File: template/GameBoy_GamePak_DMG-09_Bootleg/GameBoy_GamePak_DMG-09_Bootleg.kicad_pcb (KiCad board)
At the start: 2 copper layers, 53 x 60.7 mm, 1 part, among them J1 GameBoy_GamePak_DMG-09

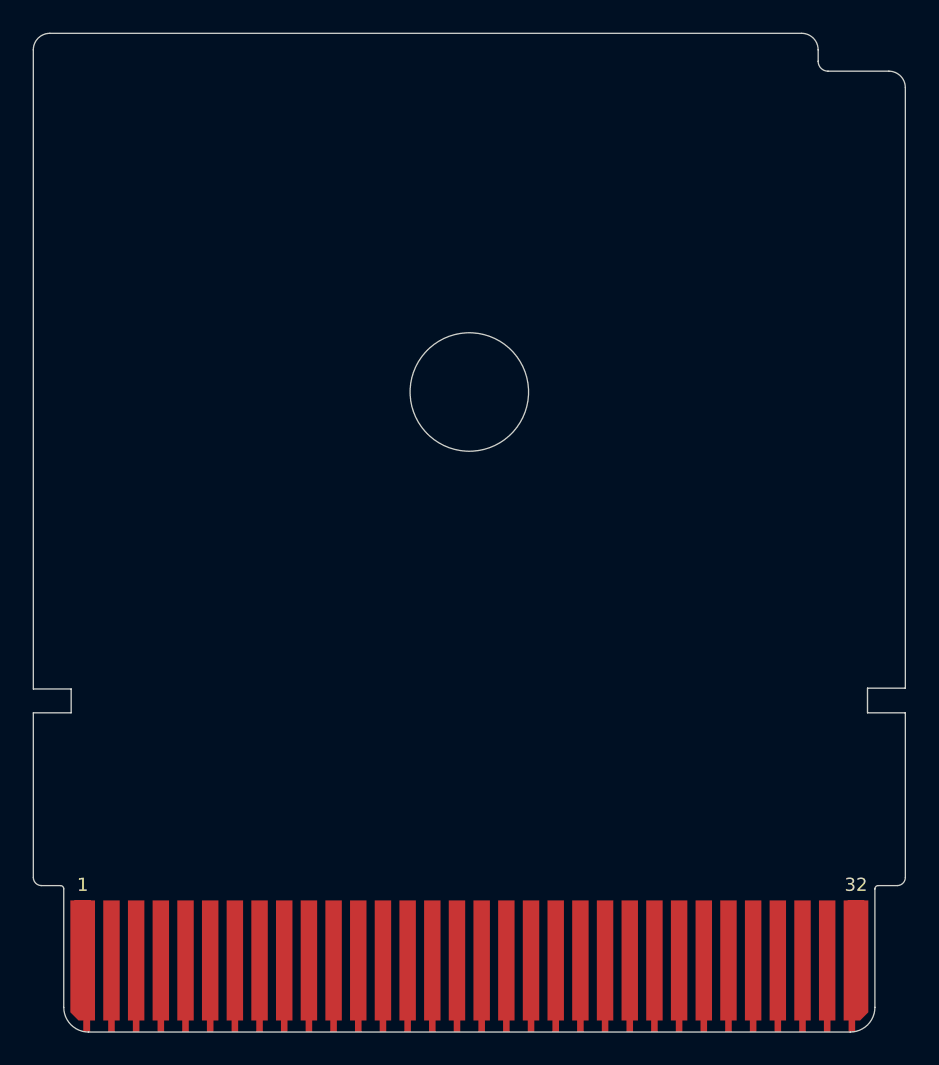
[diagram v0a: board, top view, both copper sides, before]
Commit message: Update all files to KiCAD 6.x format
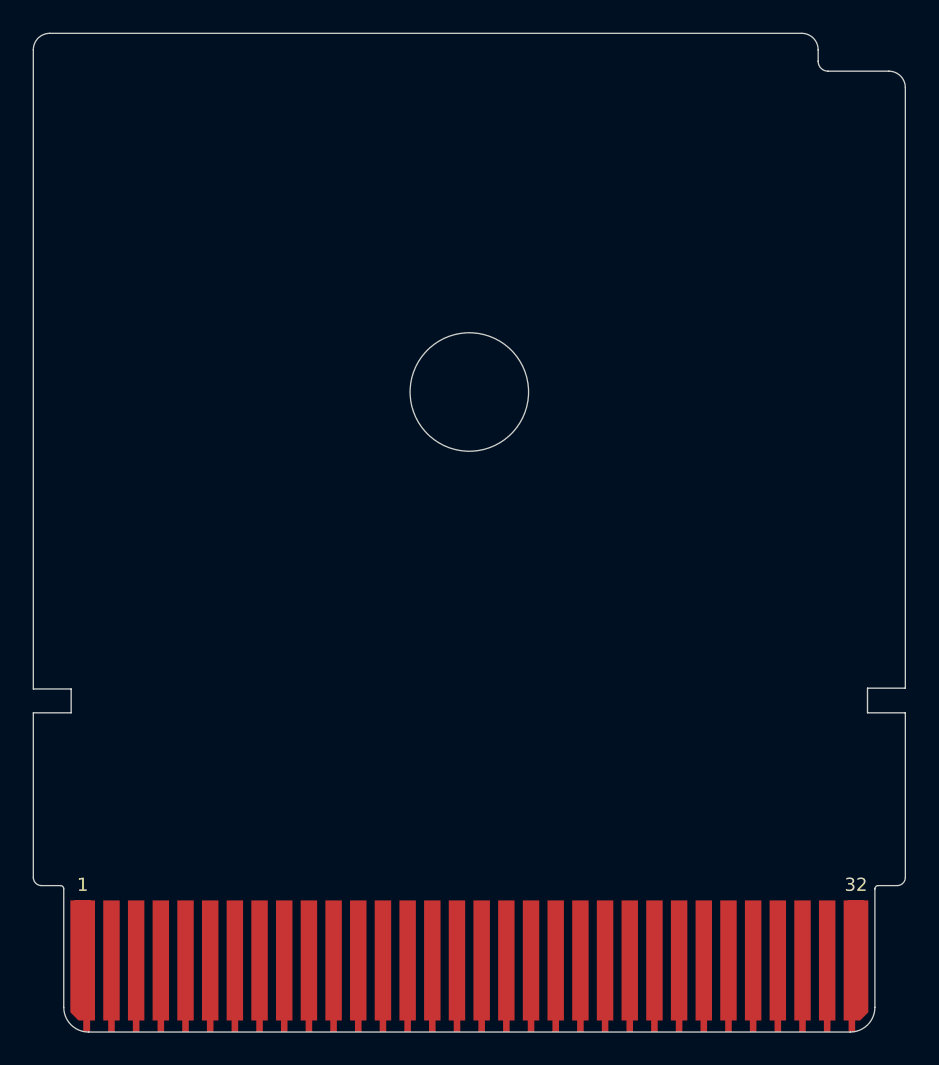
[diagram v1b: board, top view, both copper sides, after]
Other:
- net class Default removed
